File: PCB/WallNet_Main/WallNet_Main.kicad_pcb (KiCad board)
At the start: 4 copper layers, 120.6 x 69.8 mm, 87 parts, among them J1 Conn_01x05_Pin, J101 USB_C_Receptacle_PowerOnly_6P, J102 Conn_01x04_Pin, J201 Conn_01x04_Pin, J202 Conn_01x07_Socket, J203 Conn_02x12_Counter_Clockwise, Q201 BSS138, SW1 SW, U1 BT832, U101 BQ25895RTWT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

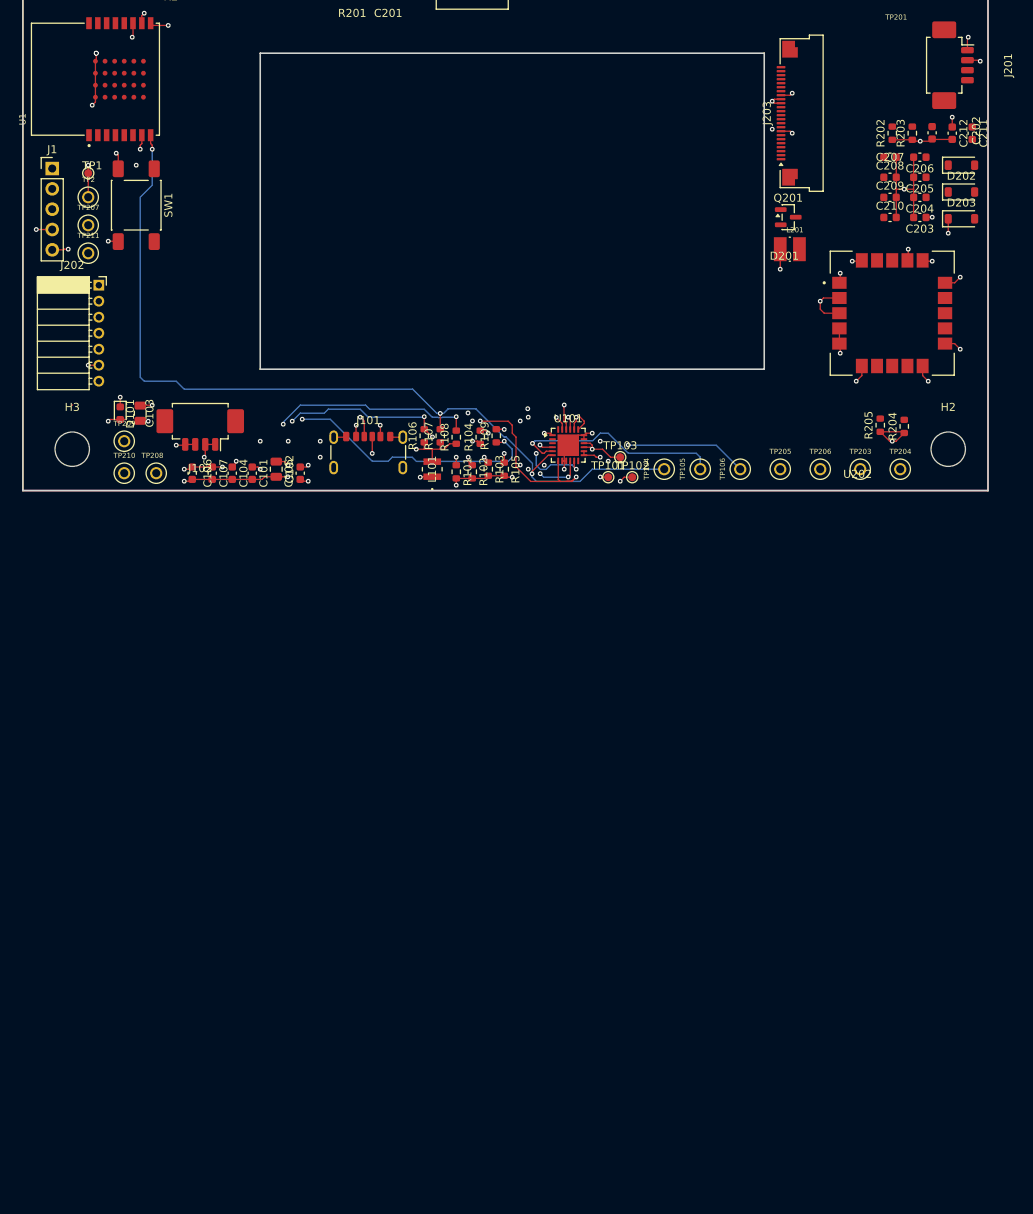
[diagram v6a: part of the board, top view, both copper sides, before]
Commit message: updated connectors, added layout guide
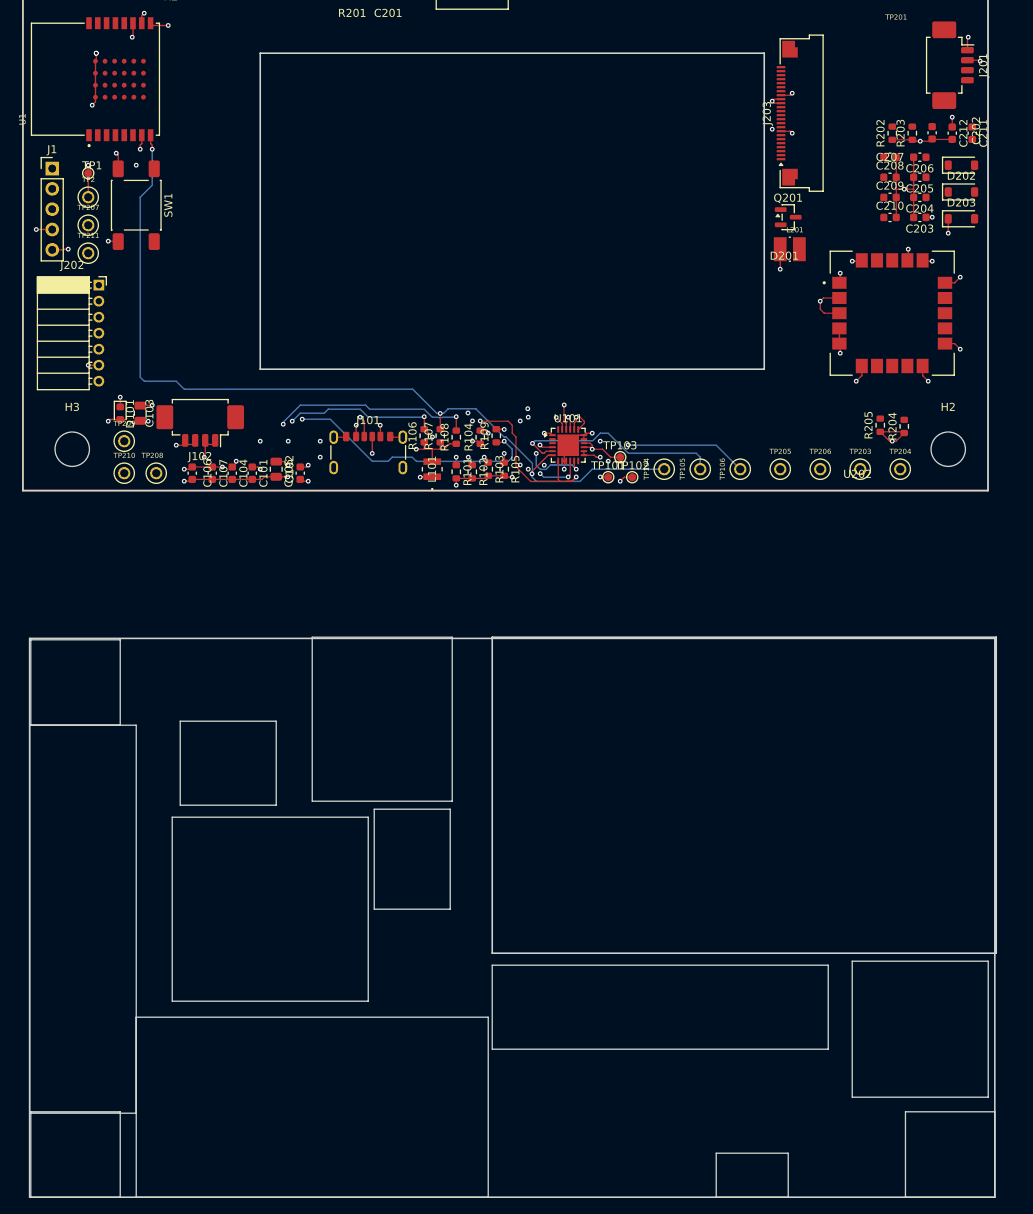
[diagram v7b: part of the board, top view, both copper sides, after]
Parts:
- J102, J201: value Conn_01x04_Pin -> 01x04 Molex
- J203: value Conn_02x12_Counter_Clockwise -> 02x12 Connector
- moved J102 0.50 mm to (33.5, 73.0)
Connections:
- J102 pad MP: (no net) -> GND
- J201 pad 1: GND -> /P11
- J201 pad 2: VDD_nrf -> /P12
- J201 pad 3: /P12 -> VDD_nrf
- J201 pad 4: /P11 -> GND
- J201 pad MP: (no net) -> GND
- J203 pad MP: (no net) -> GND
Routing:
- net GND: track 117.2 -> 115.5 mm
- net /P11: track 0.00 -> 1.67 mm
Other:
- board size 120.6 x 69.8 mm -> 121.7 x 158.2 mm
- board text added: "BQ + Components"
- board text added: "Battery"
- board text added: "Button"
- board text added: "Buzzer"
- board text added: "EINK + components"
- board text added: "FingerPrint Molex + USBC"
- board text added: "GPS"
- board text added: "MH"
- board text added: "Microcontroller"
- board text added: "Molex Batt"
- board text added: "RFID TEMPORARY"

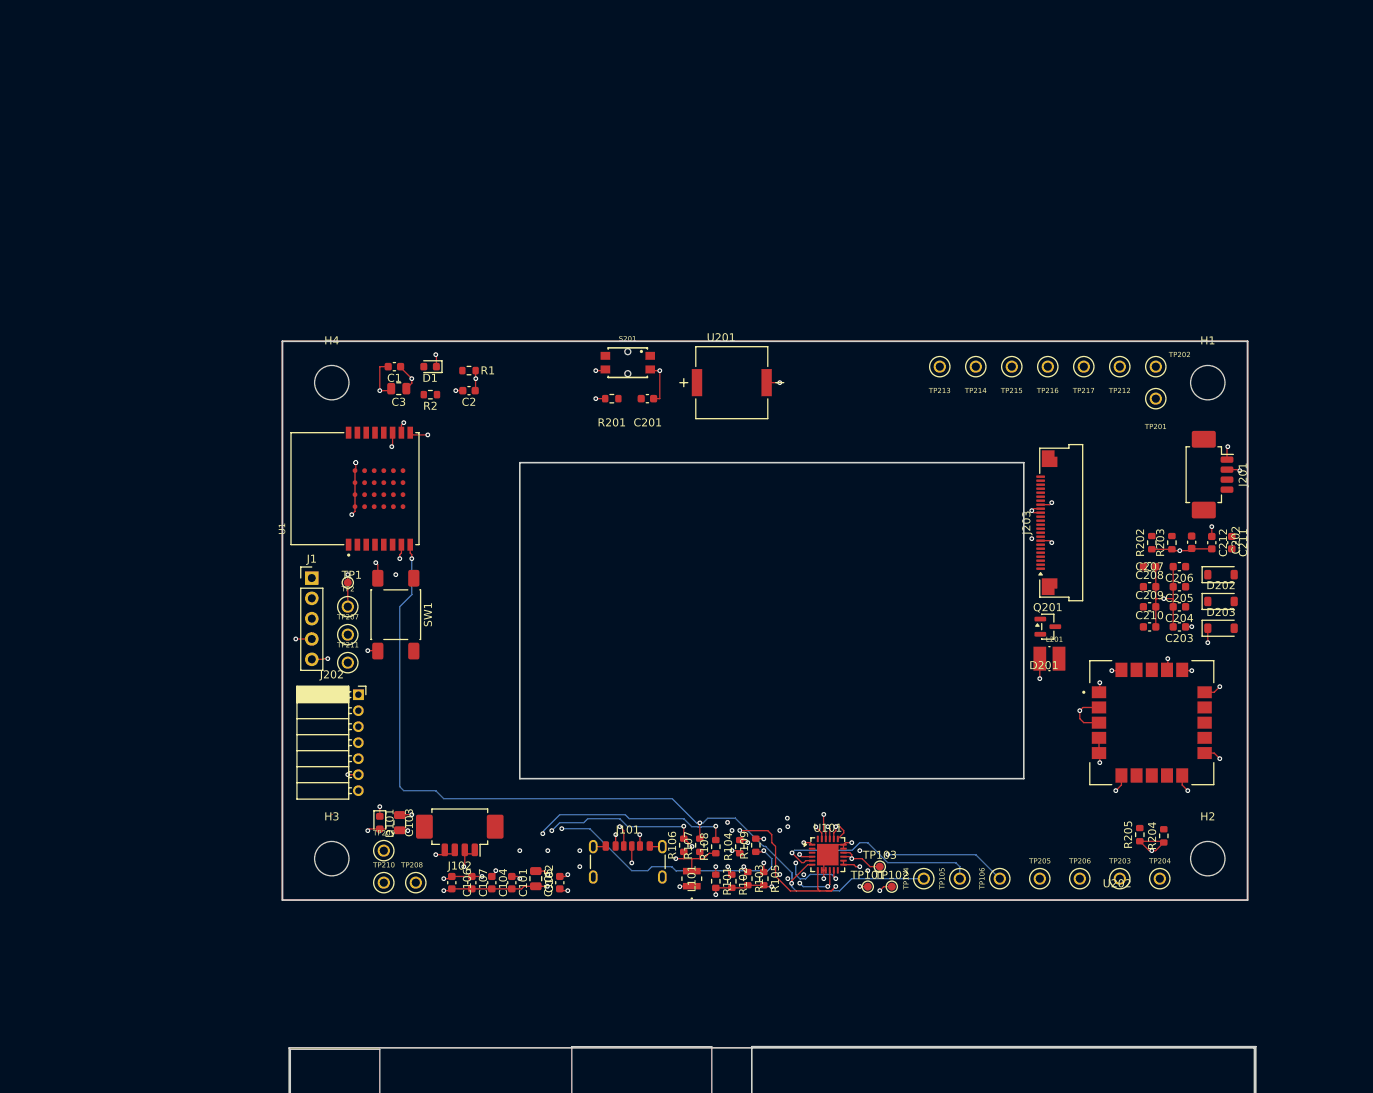
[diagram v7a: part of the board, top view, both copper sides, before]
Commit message: Reordered the parts, battery in corner, and added discreet parts next to the plug in for eink
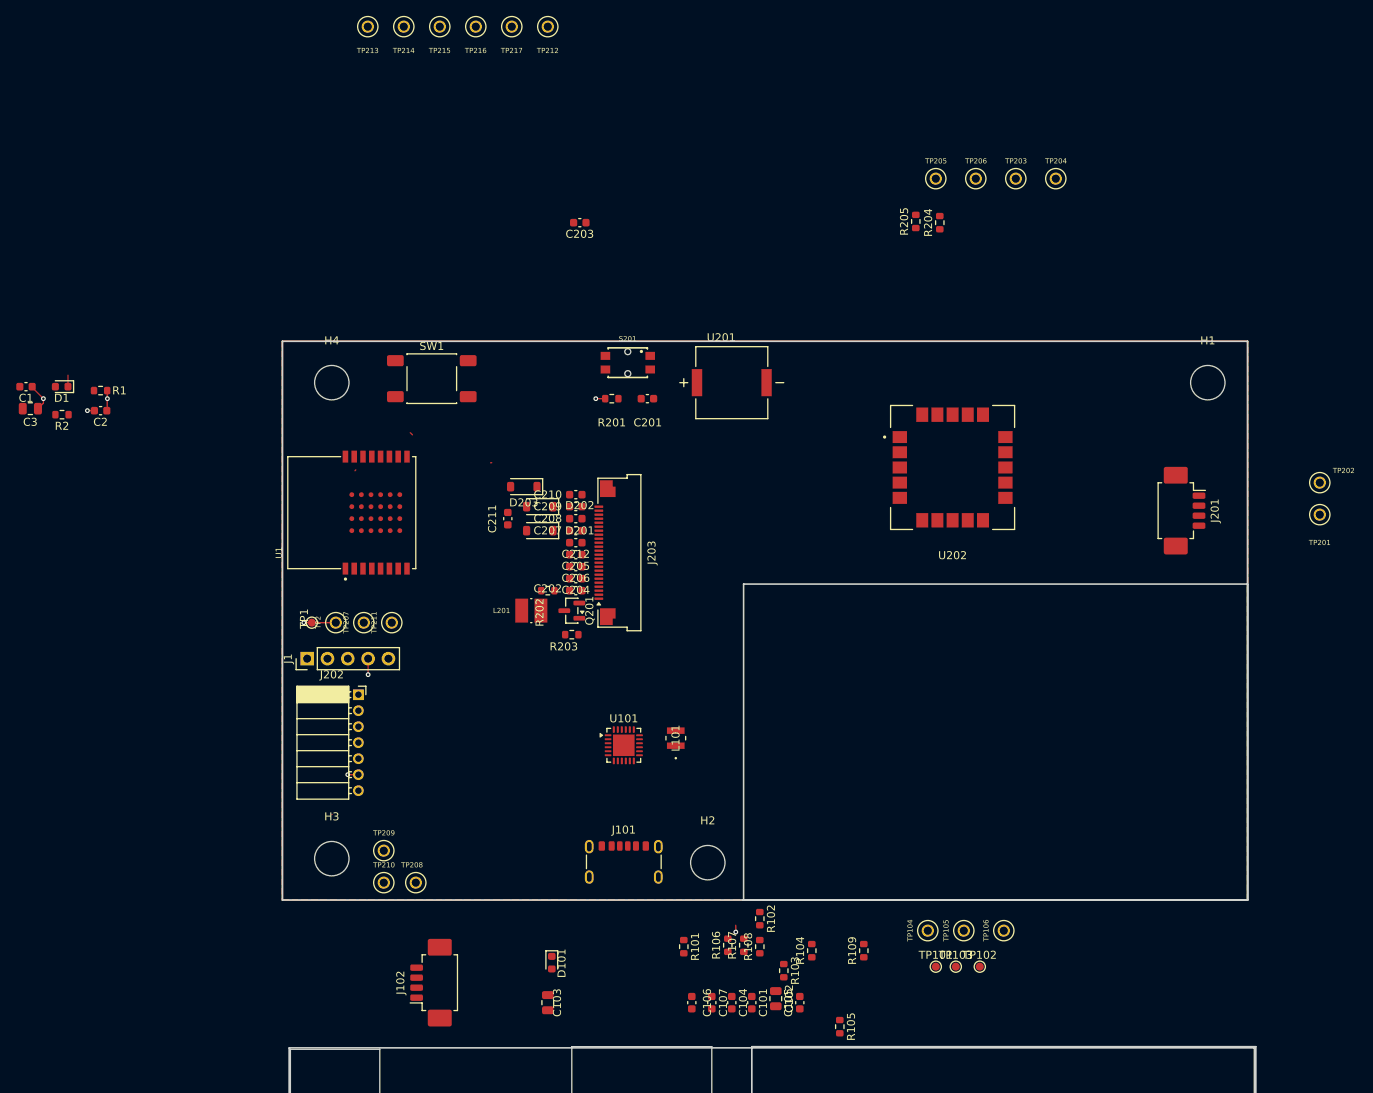
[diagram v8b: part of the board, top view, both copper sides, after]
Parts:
- moved C211 90.5 mm to (39.5, 34.0), turned to 90 degrees
- moved C203 90.4 mm to (48.5, -3.00)
- moved D203 88.9 mm to (41.5, 30.0), turned to 180 degrees
- moved TP203 88.5 mm to (103.0, -8.50)
- moved TP204 88.5 mm to (108.0, -8.50)
- moved TP205 88.5 mm to (93.0, -8.50)
- moved TP206 88.5 mm to (98.0, -8.50)
- moved D202 86.0 mm to (43.5, 32.5), turned to 180 degrees
- moved D201 85.3 mm to (43.5, 35.5), turned to 180 degrees
- moved TP212 83.2 mm to (44.5, -27.5)
- moved TP213 83.2 mm to (22.0, -27.5)
- moved TP214 83.2 mm to (26.5, -27.5)
- moved TP215 83.2 mm to (31.0, -27.5)
- moved TP216 83.2 mm to (35.5, -27.5)
- moved TP217 83.2 mm to (40.0, -27.5)
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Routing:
- net VDD_nrf: track 370.8 -> 12.1 mm, vias 20 -> 5
- net /P13: track 144.2 -> 0.00 mm, vias 8 -> 0
- net /P09: track 124.2 -> 0.00 mm, vias 5 -> 0
- net /P10: track 109.7 -> 0.00 mm, vias 3 -> 0
- net GND: track 115.5 -> 7.73 mm, vias 36 -> 3
- net /Battery/BAT: track 80.7 -> 0.00 mm, vias 5 -> 0
- net /Battery/VBUS_BQ: track 63.8 -> 0.00 mm, vias 8 -> 0
- net Net-(D101-K): track 60.9 -> 0.00 mm, vias 3 -> 0
- net /Battery/REGN: track 52.1 -> 0.00 mm, vias 5 -> 0
- net /Battery/SW: track 48.3 -> 0.00 mm, vias 5 -> 0
- net /Battery/BTST: track 43.4 -> 0.00 mm, vias 4 -> 0
- net /Battery/PMID: track 42.6 -> 0.00 mm, vias 4 -> 0
- net Net-(J101-CC1): track 23.5 -> 0.00 mm, vias 3 -> 0
- net /Battery/TS: track 18.8 -> 0.00 mm, vias 4 -> 0
- net /Battery/ILIM: track 15.4 -> 0.00 mm, vias 3 -> 0
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- added copper zone on B.Cu, net GND
- added copper zone on F.Cu, net GND
- added copper zone on In1.Cu, net VDD_nrf
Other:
- outline, holes or cut-outs redrawn
